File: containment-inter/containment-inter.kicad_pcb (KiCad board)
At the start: 2 copper layers, 25.4 x 25.4 mm, 1 part

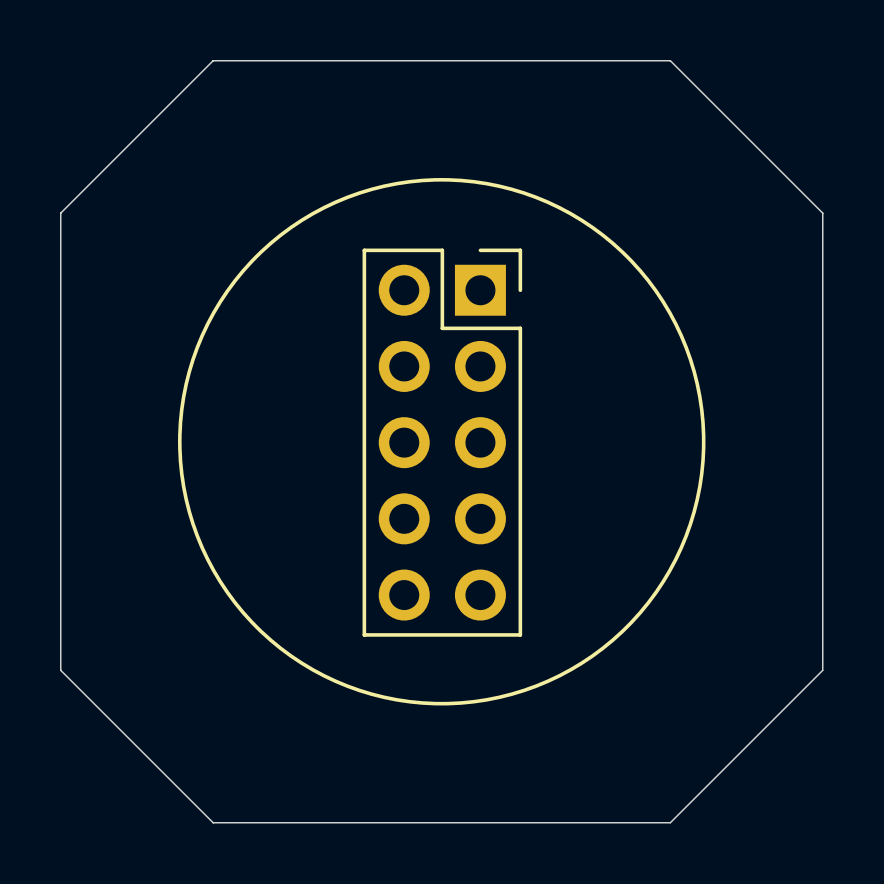
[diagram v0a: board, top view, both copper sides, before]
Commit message: containment schematic updated to include experiment & correct voltage on valve mosfets
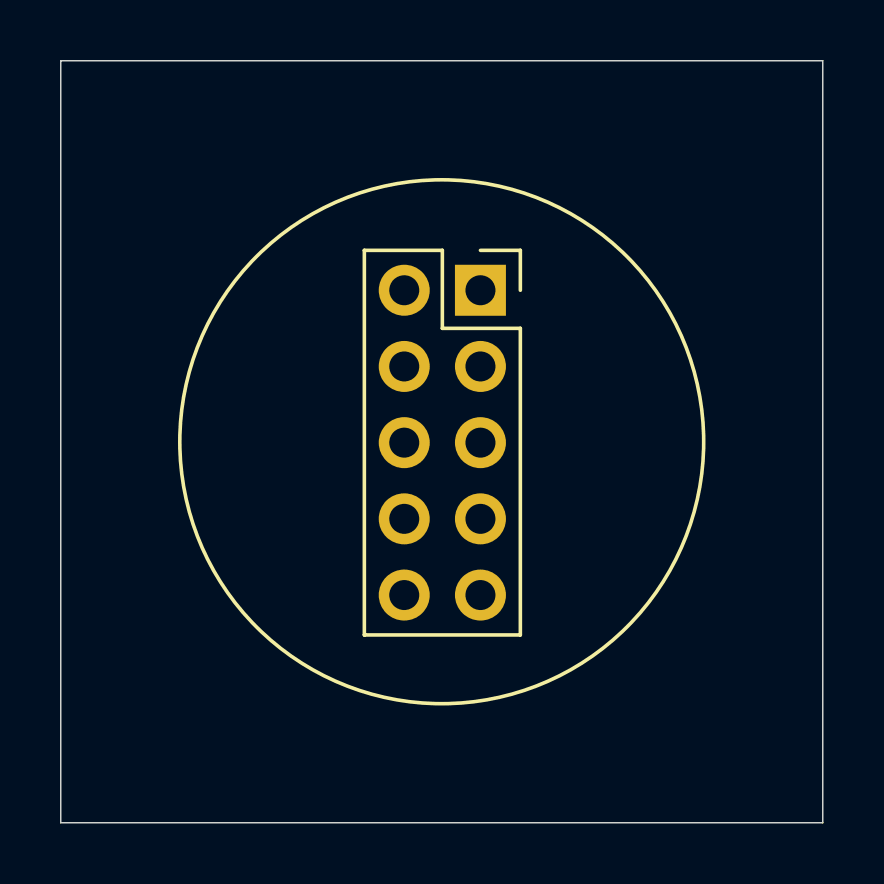
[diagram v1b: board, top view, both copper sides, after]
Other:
- outline, holes or cut-outs redrawn
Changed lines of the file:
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@@
-(kicad_pcb (version 20171130) (host pcbnew 5.1.8+dfsg1-1+b1)
+(kicad_pcb (version 20171130) (host pcbnew 5.1.9+dfsg1-1)
   (general
     (thickness 1.6)
-    (drawings 9)
+    (drawings 5)
     (tracks 0)
     (zones 0)
@@
       (effects (font (size 1 1) (thickness 0.15)))
     )
+    (fp_line (start -4.34 11.9) (end -4.34 -1.8) (layer F.CrtYd) (width 0.05))
+    (fp_line (start 1.76 11.9) (end -4.34 11.9) (layer F.CrtYd) (width 0.05))
+    (fp_line (start 1.76 -1.8) (end 1.76 11.9) (layer F.CrtYd) (width 0.05))
+    (fp_line (start -4.34 -1.8) (end 1.76 -1.8) (layer F.CrtYd) (width 0.05))
+    (fp_line (start 0 -1.33) (end 1.33 -1.33) (layer F.SilkS) (width 0.12))
+    (fp_line (start 1.33 -1.33) (end 1.33 0) (layer F.SilkS) (width 0.12))
+    (fp_line (start -1.27 -1.33) (end -1.27 1.27) (layer F.SilkS) (width 0.12))
+    (fp_line (start -1.27 1.27) (end 1.33 1.27) (layer F.SilkS) (width 0.12))
+    (fp_line (start 1.33 1.27) (end 1.33 11.49) (layer F.SilkS) (width 0.12))
+    (fp_line (start -3.87 11.49) (end 1.33 11.49) (layer F.SilkS) (width 0.12))
+    (fp_line (start -3.87 -1.33) (end -3.87 11.49) (layer F.SilkS) (width 0.12))
+    (fp_line (start -3.87 -1.33) (end -1.27 -1.33) (layer F.SilkS) (width 0.12))
+    (fp_line (start -3.81 11.43) (end -3.81 -1.27) (layer F.Fab) (width 0.1))
+    (fp_line (start 1.27 11.43) (end -3.81 11.43) (layer F.Fab) (width 0.1))
+    (fp_line (start 1.27 -0.27) (end 1.27 11.43) (layer F.Fab) (width 0.1))
+    (fp_line (start 0.27 -1.27) (end 1.27 -0.27) (layer F.Fab) (width 0.1))
     (fp_line (start -3.81 -1.27) (end 0.27 -1.27) (layer F.Fab) (width 0.1))
-    (fp_line (start 0.27 -1.27) (end 1.27 -0.27) (layer F.Fab) (width 0.1))
-    (fp_line (start 1.27 -0.27) (end 1.27 11.43) (layer F.Fab) (width 0.1))
-    (fp_line (start 1.27 11.43) (end -3.81 11.43) (layer F.Fab) (width 0.1))
-    (fp_line (start -3.81 11.43) (end -3.81 -1.27) (layer F.Fab) (width 0.1))
-    (fp_line (start -3.87 -1.33) (end -1.27 -1.33) (layer F.SilkS) (width 0.12))
-    (fp_line (start -3.87 -1.33) (end -3.87 11.49) (layer F.SilkS) (width 0.12))
-    (fp_line (start -3.87 11.49) (end 1.33 11.49) (layer F.SilkS) (width 0.12))
-    (fp_line (start 1.33 1.27) (end 1.33 11.49) (layer F.SilkS) (width 0.12))
-    (fp_line (start -1.27 1.27) (end 1.33 1.27) (layer F.SilkS) (width 0.12))
-    (fp_line (start -1.27 -1.33) (end -1.27 1.27) (layer F.SilkS) (width 0.12))
-    (fp_line (start 1.33 -1.33) (end 1.33 0) (layer F.SilkS) (width 0.12))
-    (fp_line (start 0 -1.33) (end 1.33 -1.33) (layer F.SilkS) (width 0.12))
-    (fp_line (start -4.34 -1.8) (end 1.76 -1.8) (layer F.CrtYd) (width 0.05))
-    (fp_line (start 1.76 -1.8) (end 1.76 11.9) (layer F.CrtYd) (width 0.05))
-    (fp_line (start 1.76 11.9) (end -4.34 11.9) (layer F.CrtYd) (width 0.05))
-    (fp_line (start -4.34 11.9) (end -4.34 -1.8) (layer F.CrtYd) (width 0.05))
     (fp_text user %R (at 1 5 90) (layer F.Fab)
       (effects (font (size 1 1) (thickness 0.15)))
@@
     (pad 2 thru_hole oval (at -2.54 0) (size 1.7 1.7) (drill 1) (layers *.Cu *.Mask))
     (pad 1 thru_hole rect (at 0 0) (size 1.7 1.7) (drill 1) (layers *.Cu *.Mask))
-    (model ${KIPRJMOD}/ESQ-105-13-L-D.stp
-      (offset (xyz -1.27 -5.08 2.54))
+    (model ${KIPRJMOD}/SSQ-105-03-T-D.stp
+      (offset (xyz -1.27 -5.08 0.04))
       (scale (xyz 1 1 1))
       (rotate (xyz -90 0 90))
     )
   )
-  (gr_line (start 182.88 121.92) (end 187.96 127) (layer Edge.Cuts) (width 0.05))
-  (gr_line (start 167.64 121.92) (end 162.56 127) (layer Edge.Cuts) (width 0.05))
-  (gr_line (start 167.64 147.32) (end 162.56 142.24) (layer Edge.Cuts) (width 0.05))
-  (gr_line (start 187.96 142.24) (end 182.88 147.32) (layer Edge.Cuts) (width 0.05))
   (gr_circle (center 175.26 134.62) (end 183.99125 134.62) (layer F.SilkS) (width 0.12))
-  (gr_line (start 162.56 142.24) (end 162.56 127) (layer Edge.Cuts) (width 0.05))
-  (gr_line (start 182.88 147.32) (end 167.64 147.32) (layer Edge.Cuts) (width 0.05))
-  (gr_line (start 187.96 127) (end 187.96 142.24) (layer Edge.Cuts) (width 0.05))
-  (gr_line (start 167.64 121.92) (end 182.88 121.92) (layer Edge.Cuts) (width 0.05))
+  (gr_line (start 162.56 147.32) (end 162.56 121.92) (layer Edge.Cuts) (width 0.05))
+  (gr_line (start 187.96 147.32) (end 162.56 147.32) (layer Edge.Cuts) (width 0.05))
+  (gr_line (start 187.96 121.92) (end 187.96 147.32) (layer Edge.Cuts) (width 0.05))
+  (gr_line (start 162.56 121.92) (end 187.96 121.92) (layer Edge.Cuts) (width 0.05))
 )
